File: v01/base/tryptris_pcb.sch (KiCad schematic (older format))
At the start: 132 parts, among them J1 USB_C_Receptacle_USB2.0, J2 I2C-L, J3 I2C-R, J4 AVR-ISP-6, SW1 Reset, U1 ATmega32U4-AU, U2 MCP23017_SO, Y1 16Mhz

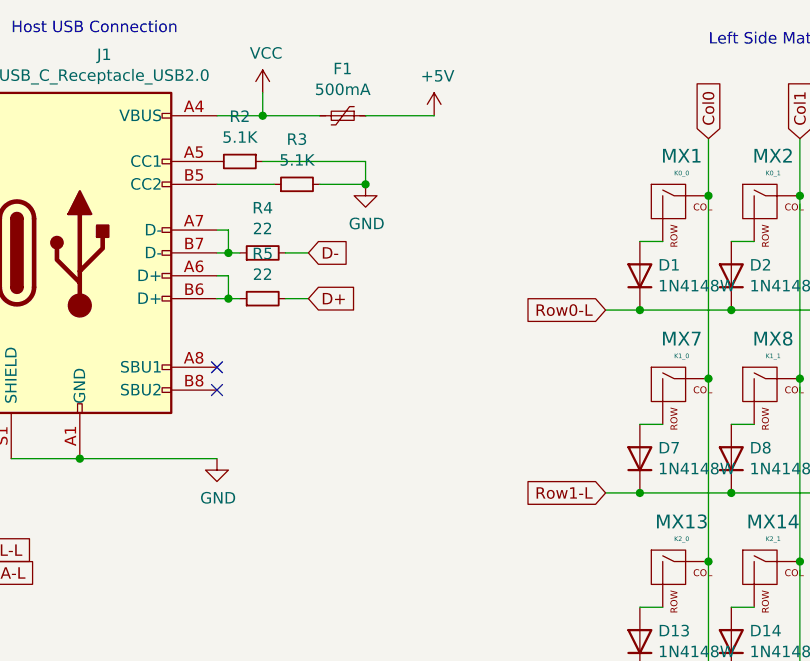
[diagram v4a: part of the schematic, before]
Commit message: Add ESD component to both boards.
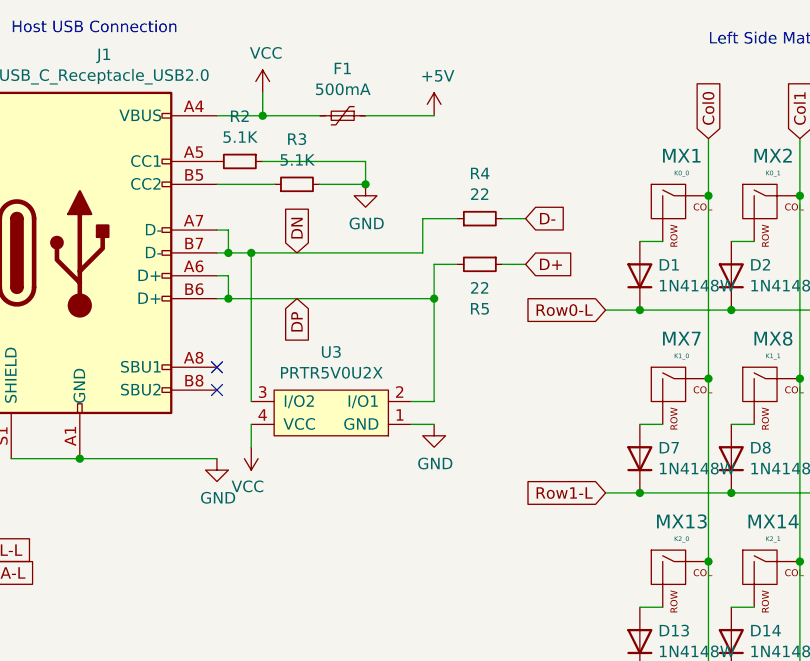
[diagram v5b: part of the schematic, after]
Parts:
- added U3: PRTR5V0U2X, Keebio-Parts:SOT-143B, symbol keebio:PRTR5V0U2X
- F1: footprint Fuse:Fuse_0805_2012Metric_Pad1.15x1.40mm_HandSolder -> Fuse:Fuse_1206_3216Metric_Pad1.42x1.75mm_HandSolder
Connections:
- net D+: now also R5.1; no longer R5.2
- net GND: now also U3.1 (GND)
- net VCC: now also U3.4 (VCC)
- net DP: now reaches J1.A6 (D+), J1.B6 (D+)
- net DP: now also R5.2, U3.2 (I/O1); no longer R5.1
- net DN: now reaches J1.A7 (D-), J1.B7 (D-), R4.1
- net DN: now also U3.3 (I/O2)
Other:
- moved on the sheet: R4, R5
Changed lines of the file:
@@
 F 0 "F1" V 6045 1050 50  0000 C CNN
 F 1 "500mA" V 6136 1050 50  0000 C CNN
-F 2 "Fuse:Fuse_0805_2012Metric_Pad1.15x1.40mm_HandSolder" H 6300 850 50  0001 L CNN
+F 2 "Fuse:Fuse_1206_3216Metric_Pad1.42x1.75mm_HandSolder" H 6300 850 50  0001 L CNN
 F 3 "~" H 6250 1050 50  0001 C CNN
 	1    6250 1050
@@
 L Device:R_Small R4
 U 1 1 61EF46E6
-P 5900 1650
-F 0 "R4" V 6096 1650 50  0000 C CNN
-F 1 "22" V 6005 1650 50  0000 C CNN
-F 2 "Resistor_SMD:R_0805_2012Metric" H 5900 1650 50  0001 C CNN
-F 3 "~" H 5900 1650 50  0001 C CNN
-	1    5900 1650
+P 6850 1500
+F 0 "R4" V 7046 1500 50  0000 C CNN
+F 1 "22" V 6955 1500 50  0000 C CNN
+F 2 "Resistor_SMD:R_0805_2012Metric" H 6850 1500 50  0001 C CNN
+F 3 "~" H 6850 1500 50  0001 C CNN
+	1    6850 1500
 	0    -1   -1   0
 $EndComp
@@
 	5750 1550 5750 1650
 Connection ~ 5750 1650
-Wire Wire Line
-	5750 1650 5800 1650
-Text GLabel 6100 1650 2    50   Input ~ 0
+Text GLabel 7050 1500 2    50   Input ~ 0
 D-
 Wire Wire Line
-	6000 1650 6100 1650
+	6950 1500 7050 1500
 $Comp
 L Device:R_Small R5
 U 1 1 61F3054F
-P 5900 1850
-F 0 "R5" V 6096 1850 50  0000 C CNN
-F 1 "22" V 6005 1850 50  0000 C CNN
-F 2 "Resistor_SMD:R_0805_2012Metric" H 5900 1850 50  0001 C CNN
-F 3 "~" H 5900 1850 50  0001 C CNN
-	1    5900 1850
-	0    -1   -1   0
+P 6850 1700
+F 0 "R5" V 7046 1700 50  0000 C CNN
+F 1 "22" V 6955 1700 50  0000 C CNN
+F 2 "Resistor_SMD:R_0805_2012Metric" H 6850 1700 50  0001 C CNN
+F 3 "~" H 6850 1700 50  0001 C CNN
+	1    6850 1700
+	0    1    1    0
 $EndComp
 Wire Wire Line
@@
 Wire Wire Line
 	5750 1750 5750 1850
-Connection ~ 5750 1850
-Wire Wire Line
-	5750 1850 5800 1850
-Text GLabel 6100 1850 2    50   Input ~ 0
+Text GLabel 7050 1700 2    50   Input ~ 0
 D+
 Wire Wire Line
-	6000 1850 6100 1850
+	6950 1700 7050 1700
 NoConn ~ 5700 2150
 NoConn ~ 5700 2250
@@
 	2000 1300 1400 1300
 Connection ~ 2400 1600
+$Comp
+L keebio:PRTR5V0U2X U3
+U 1 1 61AD454A
+P 6200 2350
+F 0 "U3" H 6200 2085 50  0000 C CNN
+F 1 "PRTR5V0U2X" H 6200 2176 50  0000 C CNN
+F 2 "Keebio-Parts:SOT-143B" H 6150 2450 50  0001 C CNN
+F 3 "" H 6150 2450 50  0001 C CNN
+	1    6200 2350
+	-1   0    0    1
+$EndComp
+Wire Wire Line
+	6550 2300 6650 2300
+Wire Wire Line
+	6650 1700 6750 1700
+$Comp
+L power:GND #PWR0130
+U 1 1 61C06BC4
+P 6650 2400
+F 0 "#PWR0130" H 6650 2150 50  0001 C CNN
+F 1 "GND" H 6655 2227 50  0000 C CNN
+F 2 "" H 6650 2400 50  0001 C CNN
+F 3 "" H 6650 2400 50  0001 C CNN
+	1    6650 2400
+	1    0    0    -1
+$EndComp
+Wire Wire Line
+	6650 2400 6550 2400
+$Comp
+L power:VCC #PWR0131
+U 1 1 61C2243A
+P 5850 2500
+F 0 "#PWR0131" H 5850 2350 50  0001 C CNN
+F 1 "VCC" H 5865 2673 50  0000 C CNN
+F 2 "" H 5850 2500 50  0001 C CNN
+F 3 "" H 5850 2500 50  0001 C CNN
+	1    5850 2500
+	-1   0    0    1
+$EndComp
+Wire Wire Line
+	5850 2500 5850 2400
+Wire Wire Line
+	6600 1650 6600 1500
+Wire Wire Line
+	6600 1500 6750 1500
+Wire Wire Line
+	5750 1850 6650 1850
+Wire Wire Line
+	6650 1700 6650 1850
+Connection ~ 5750 1850
+Wire Wire Line
+	5750 1650 5850 1650
+Wire Wire Line
+	5850 1650 5850 2300
+Connection ~ 5850 1650
+Wire Wire Line
+	5850 1650 6600 1650
+Wire Wire Line
+	6650 1850 6650 2300
+Connection ~ 6650 1850
+Text GLabel 6050 1650 1    50   Input ~ 0
+DN
+Text GLabel 6050 1850 3    50   Input ~ 0
+DP
 $EndSCHEMATC

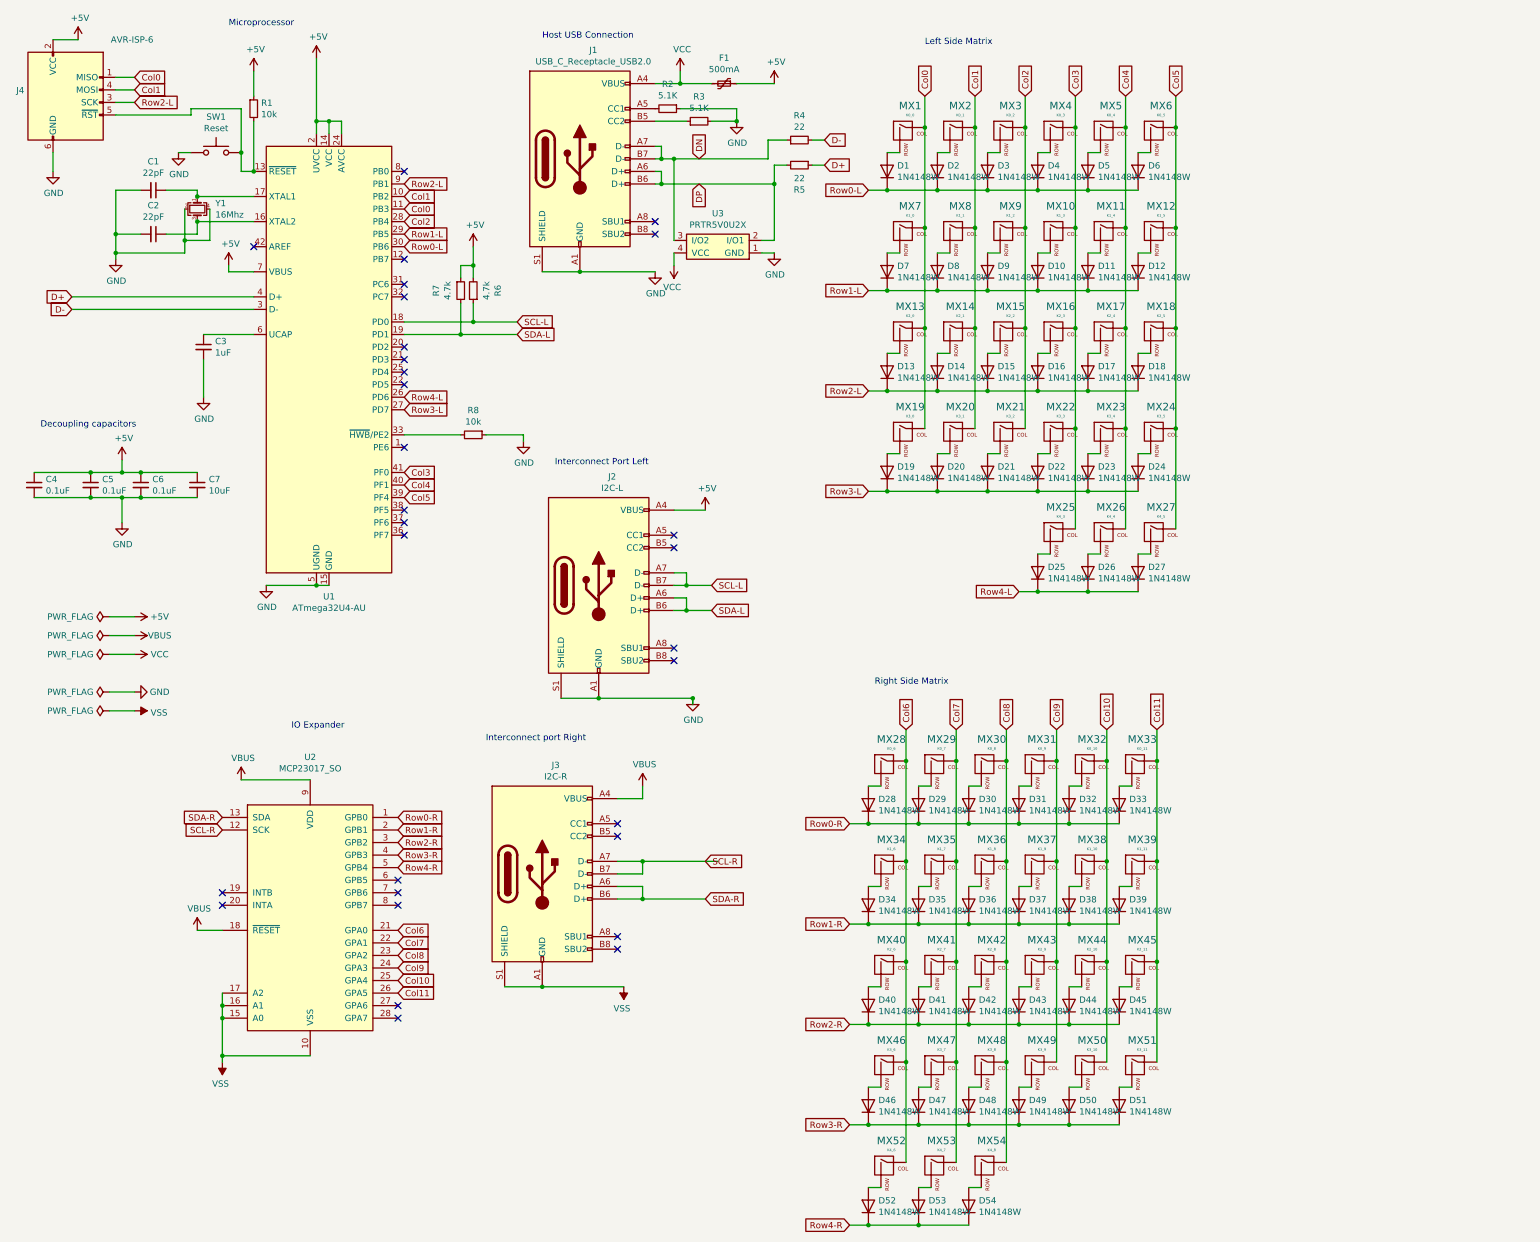
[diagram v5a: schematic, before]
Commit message: Add interconnect ESD to base.
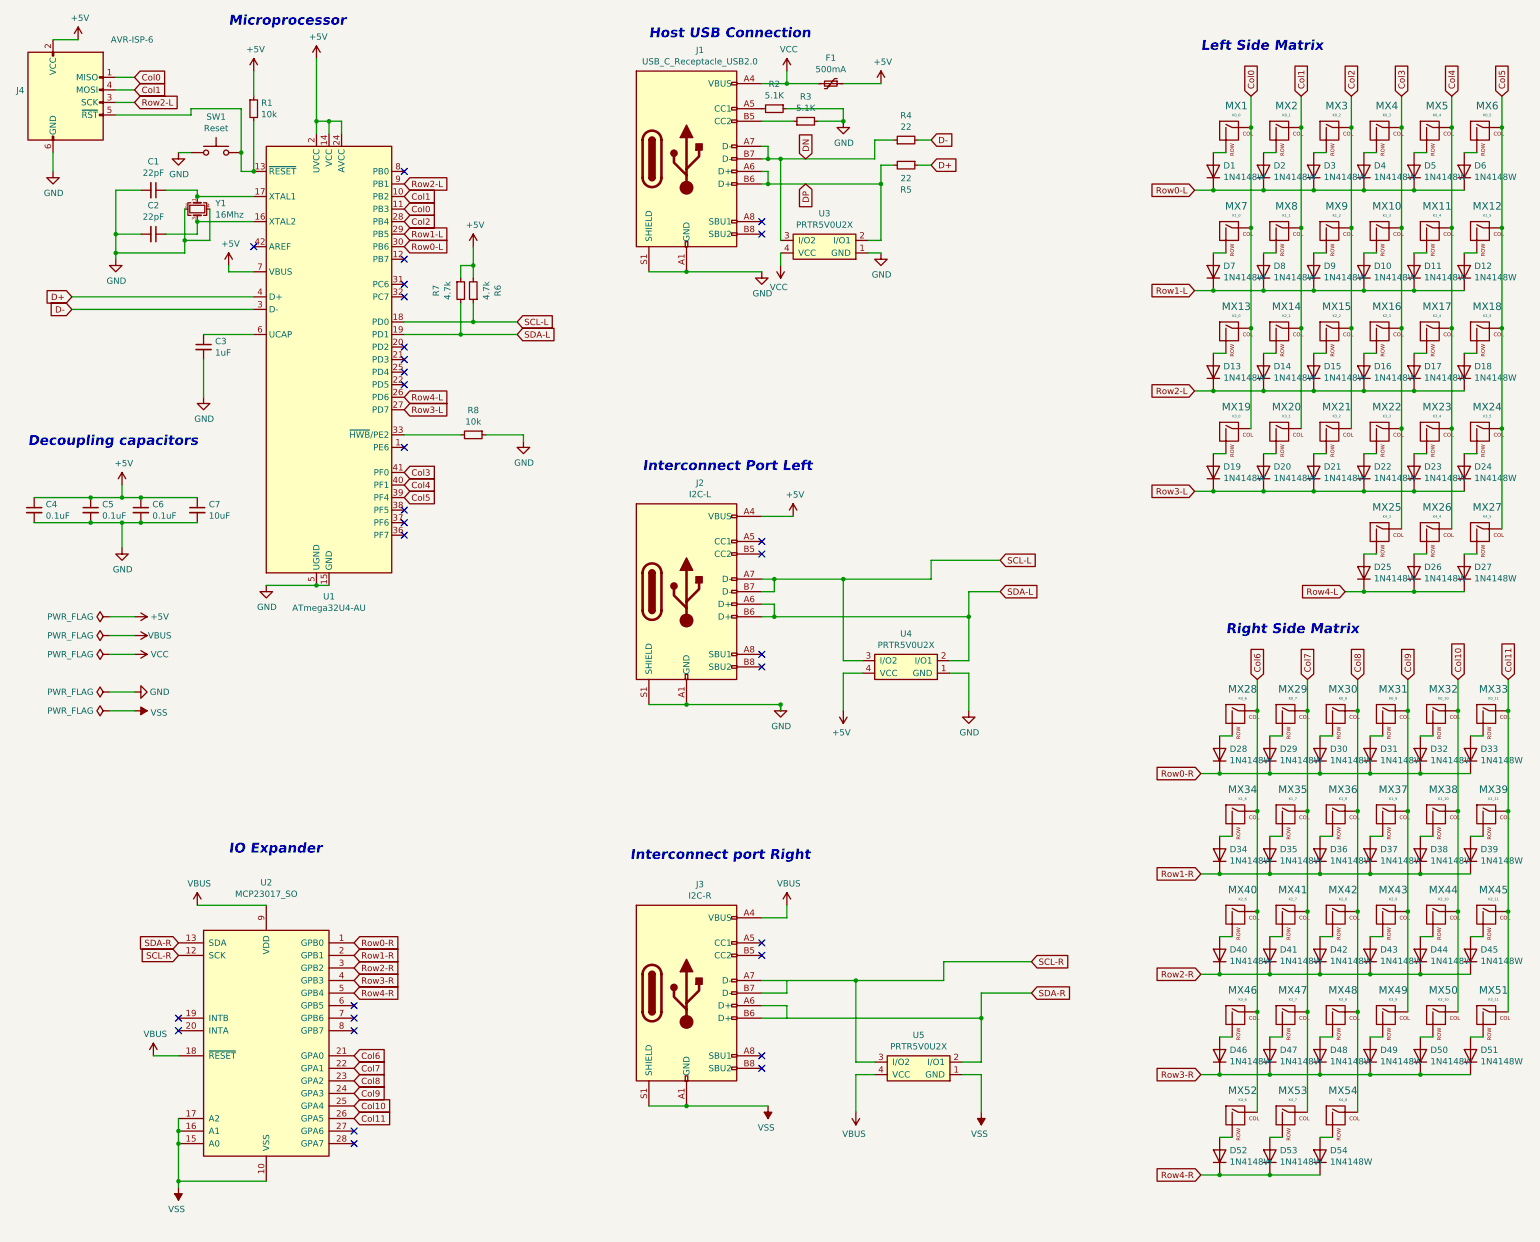
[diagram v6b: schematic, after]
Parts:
- added U4, U5: PRTR5V0U2X, Keebio-Parts:SOT-143B, symbol keebio:PRTR5V0U2X
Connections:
- net +5V: now also U4.4 (VCC)
- net GND: now also U4.1 (GND)
- net SCL-L: now also U4.3 (I/O2)
- net SCL-R: now also U5.3 (I/O2)
- net SDA-L: now also U4.2 (I/O1)
- net SDA-R: now also U5.2 (I/O1)
- net VBUS: now also U5.4 (VCC)
- net VSS: now also U5.1 (GND)
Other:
- moved on the sheet: C4, C5, C6, C7, D1, D10, D11, D12, D13, D14, D15, D16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
